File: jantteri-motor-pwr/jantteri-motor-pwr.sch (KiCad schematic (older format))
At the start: 0 parts

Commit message: jantteri-pwr-motor
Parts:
- added F1: C58066, Fuse:Fuseholder_Cylinder-5x20mm_Stelvio-Kontek_PTF78_Horizontal_Open, symbol Device:Fuse_Small
- added FB1: GZ2012D101TF, Inductor_SMD:L_0805_2012Metric, symbol Device:Ferrite_Bead
- added H1, H2, H3, H4: MountingHole_Pad, MountingHole:MountingHole_3.2mm_M3_Pad_Via, symbol Mechanical:MountingHole_Pad
- added J1: Conn_01x06_Male, Connector_JST2:JST_ZH_B6B-ZR_1x06_P1.50mm_Vertical, symbol Connector:Conn_01x06_Male
- added J5: 12V, Connector_PinHeader_2.54mm:PinHeader_1x02_P2.54mm_Vertical, symbol Connector:Conn_01x02_Male
- added J6: PWR-SW, Connector_PinHeader_2.54mm:PinHeader_1x03_P2.54mm_Vertical, symbol Connector:Conn_01x03_Male
- added J7: M, Connector_PinHeader_2.54mm:PinHeader_1x02_P2.54mm_Vertical, symbol Connector:Conn_01x02_Male
- added Q1: PDN3909S, Package_TO_SOT_SMD:SOT-23, symbol Transistor_FET:Si2319CDS
- added R1, R2: 4K7, Resistor_SMD:R_0805_2012Metric, symbol Device:R_Small
- added U1: lora-mod, voja-footprints:lora-mod, symbol voja-lib:lora-mod
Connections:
- net labels added: +3.3V, DRV_FAULT, DRV_SLEEP, HIT_INT, LORA_INT, M+, M-, MOTOR_A, MOTOR_B, POT, PWR+, SCL, SDA, USB-5V
- net labels removed: +3V3
- wire segments 8 -> 55
- no-connect marks 0 -> 2

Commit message: revised motor-pwr
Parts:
- U1: symbol voja-lib:lora-mod -> jantteri-motor-pwr-rescue:lora-mod-voja-lib
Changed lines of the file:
@@
 	2500 3750 2550 3750
 $Comp
-L voja-lib:lora-mod U1
+L jantteri-motor-pwr-rescue:lora-mod-voja-lib U1
 U 1 1 611C29AF
 P 8700 4200

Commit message: random changes
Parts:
- removed F1: C58066, Fuse:Fuseholder_Cylinder-5x20mm_Stelvio-Kontek_PTF78_Horizontal_Open, symbol Device:Fuse_Small
- Q1: value PDN3909S -> AO3401A; LCSC C441843 -> C700954
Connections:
- net PWR+: now also J6.2 (Pin_2)
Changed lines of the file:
@@
 AR Path="/612244CD/611DB1A0" Ref="Q?"  Part="1"
 F 0 "Q1" V 1492 1250 50  0000 C CNN
-F 1 "PDN3909S" V 1401 1250 50  0000 C CNN
+F 1 "AO3401A" V 1401 1250 50  0000 C CNN
 F 2 "Package_TO_SOT_SMD:SOT-23" H 1350 1175 50  0001 L CIN
 F 3 "http://www.vishay.com/docs/66709/si2319cd.pdf" H 1150 1250 50  0001 L CNN
-F 4 "C441843" V 1150 1250 50  0001 C CNN "LCSC"
+F 4 "C700954" V 1150 1250 50  0001 C CNN "LCSC"
 	1    1150 1250
 	0    -1   -1   0
@@
 	1    0    0    -1
 $EndComp
-$Comp
-L Device:Fuse_Small F1
-U 1 1 611FF9F7
-P 7750 2150
-F 0 "F1" H 7750 2335 50  0000 C CNN
-F 1 "C58066" H 7750 2244 50  0000 C CNN
-F 2 "Fuse:Fuseholder_Cylinder-5x20mm_Stelvio-Kontek_PTF78_Horizontal_Open" H 7750 2150 50  0001 C CNN
-F 3 "~" H 7750 2150 50  0001 C CNN
-F 4 "C58066" H 7750 2150 50  0001 C CNN "LCSC"
-	1    7750 2150
-	1    0    0    -1
-$EndComp
 Wire Wire Line
 	7200 2250 7500 2250
@@
 Wire Wire Line
 	7750 1600 7750 1700
-Wire Wire Line
-	7200 2150 7650 2150
-Wire Wire Line
-	7850 2150 8100 2150
 $Comp
 L Connector:Conn_01x02_Male J7
@@
 	1    0    0    -1
 $EndComp
+Wire Wire Line
+	7200 2150 8100 2150
 $EndSCHEMATC

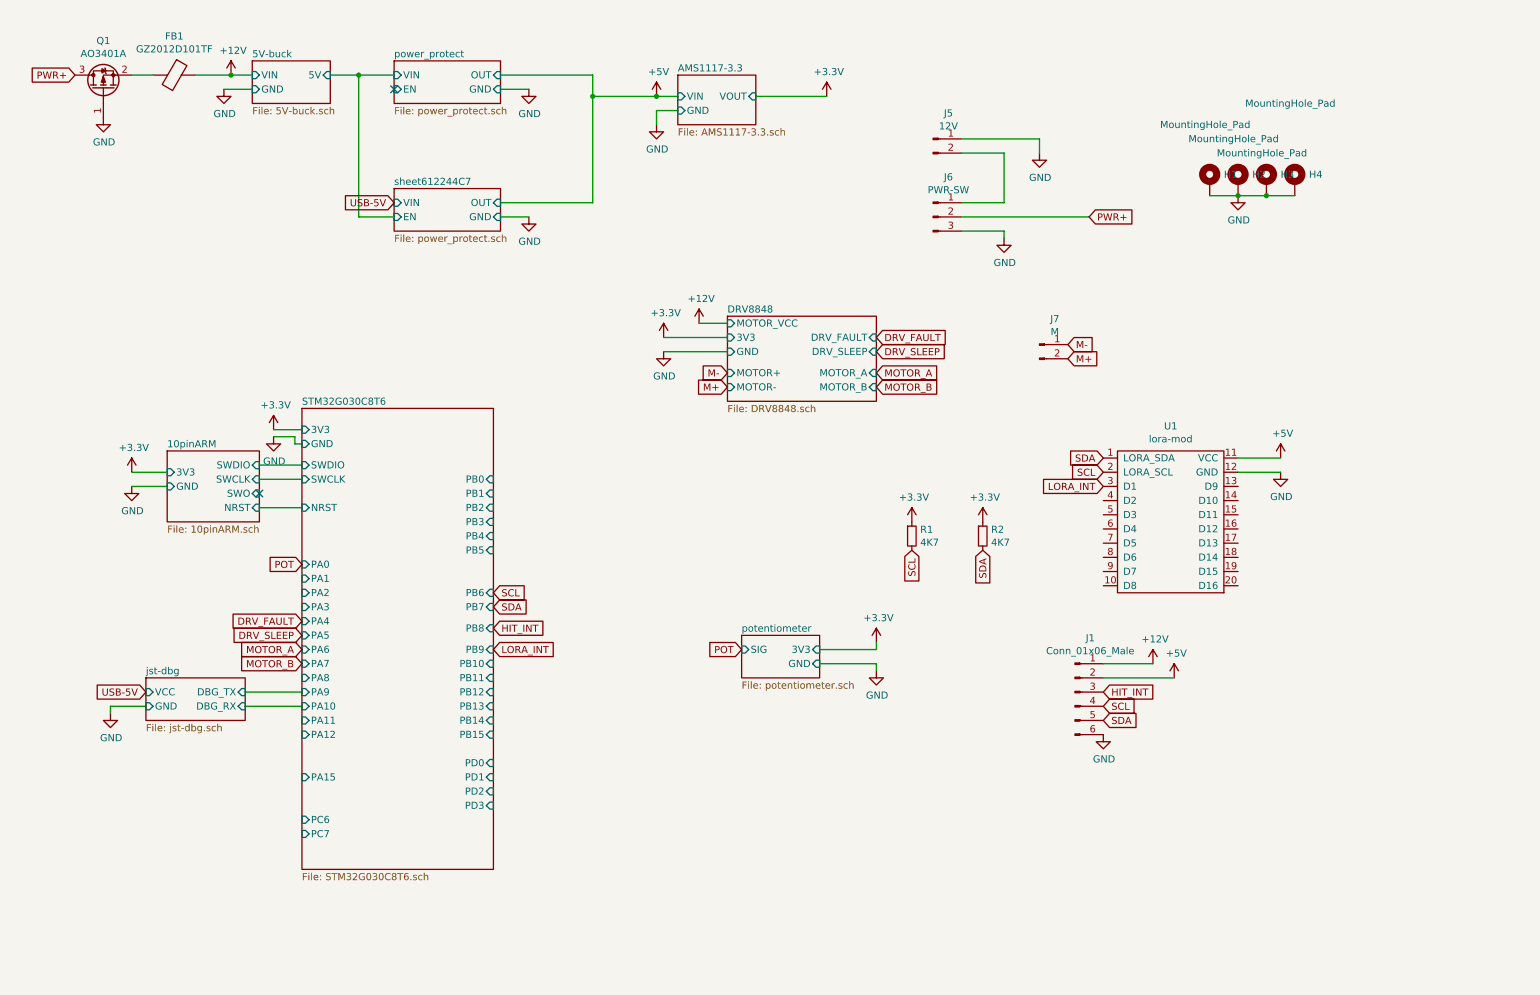
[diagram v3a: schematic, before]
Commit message: Tuubijantteri design Ordered
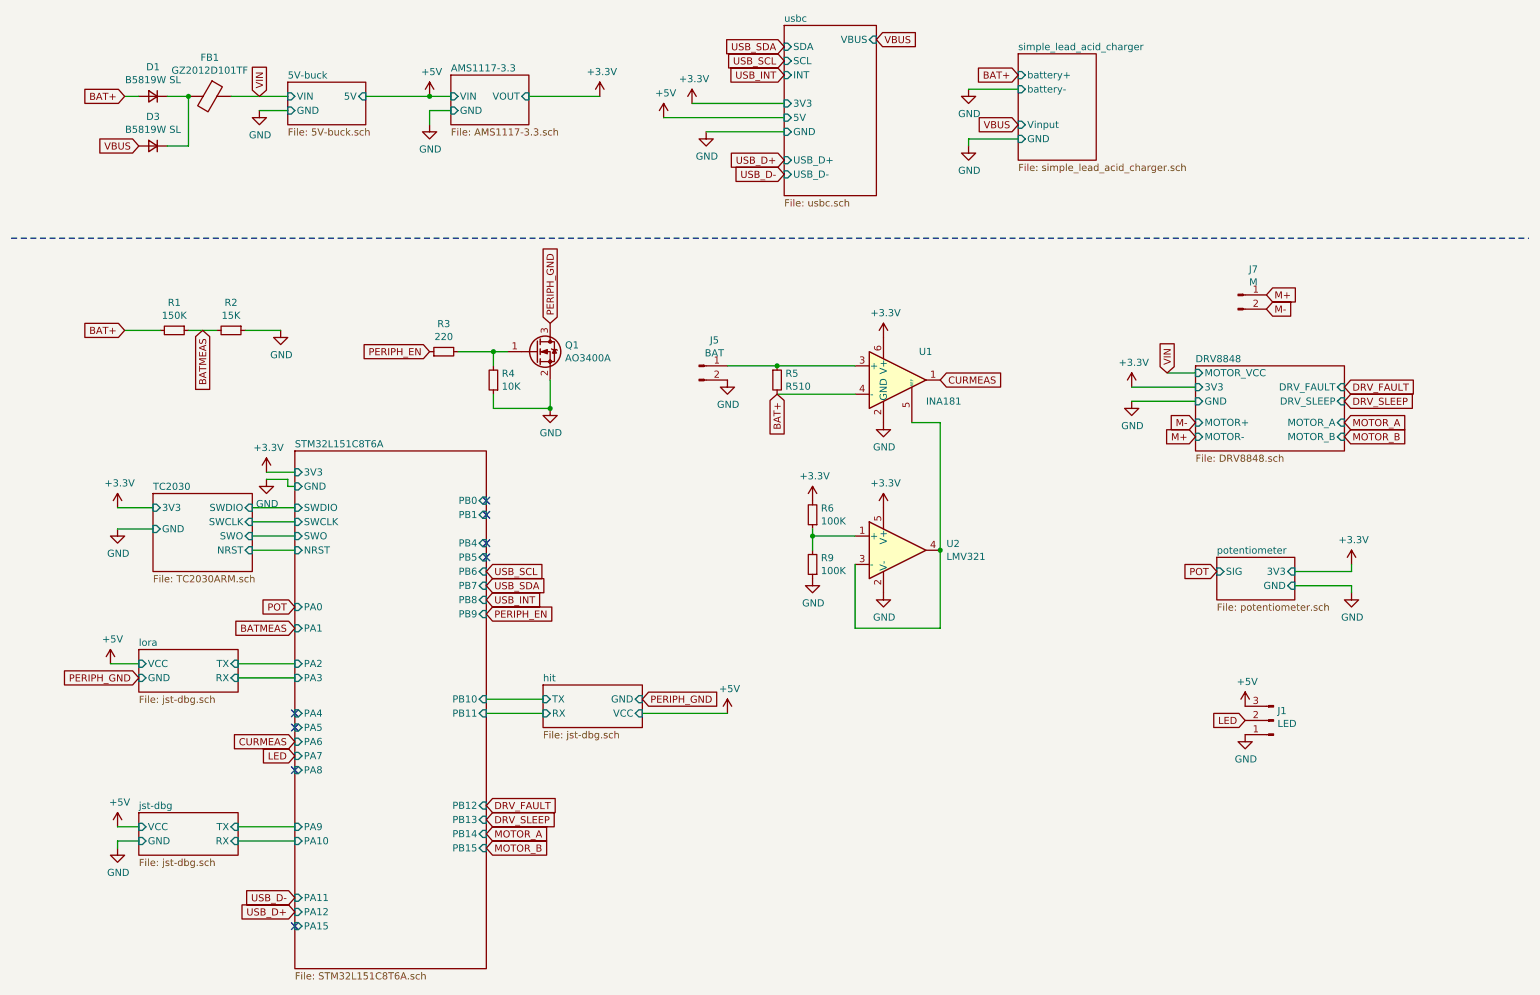
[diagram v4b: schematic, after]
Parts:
- removed H1, H2, H3, H4: MountingHole_Pad, MountingHole:MountingHole_3.2mm_M3_Pad_Via, symbol Mechanical:MountingHole_Pad
- removed J1: Conn_01x06_Male, Connector_JST2:JST_ZH_B6B-ZR_1x06_P1.50mm_Vertical, symbol Connector:Conn_01x06_Male
- removed J6: PWR-SW, Connector_PinHeader_2.54mm:PinHeader_1x03_P2.54mm_Vertical, symbol Connector:Conn_01x03_Male
- removed Q1: AO3401A, Package_TO_SOT_SMD:SOT-23, symbol Transistor_FET:Si2319CDS
- removed U1: lora-mod, voja-footprints:lora-mod, symbol jantteri-motor-pwr-rescue:lora-mod-voja-lib
- added D1, D3: B5819W SL, Diode_SMD:D_SOD-123, symbol Device:D_Small
- added J1: LED, Connector_JST2:JST_ZH_B3B-ZR_1x03_P1.50mm_Vertical, symbol Connector:Conn_01x03_Male
- added Q1: AO3400A, Package_TO_SOT_SMD:SOT-23, symbol Transistor_FET:AO3400A
- added R3: 220, Resistor_SMD:R_0402_1005Metric, symbol Device:R_Small
- added R4: 10K, Resistor_SMD:R_0402_1005Metric, symbol Device:R_Small
- added R5: R510, Resistor_SMD:R_2512_6332Metric, symbol Device:R_Small
- added R6, R9: 100K, Resistor_SMD:R_0402_1005Metric, symbol Device:R_Small
- added U1: INA181, Package_TO_SOT_SMD:SOT-23-6, symbol Amplifier_Current:INA181
- added U2: LMV321, Package_TO_SOT_SMD:SOT-23-5, symbol Amplifier_Operational:LMV321
- J5: value 12V -> BAT; footprint Connector_PinHeader_2.54mm:PinHeader_1x02_P2.54mm_Vertical -> Connector_JST2:JST_VH_B2PS-VH_1x02_P3.96mm_Horizontal
- J7: footprint Connector_PinHeader_2.54mm:PinHeader_1x02_P2.54mm_Vertical -> Connector_JST2:JST_VH_B2PS-VH_1x02_P3.96mm_Horizontal
- R1: value 4K7 -> 150K; footprint Resistor_SMD:R_0805_2012Metric -> Resistor_SMD:R_0402_1005Metric; LCSC C17673 -> C25755
- R2: value 4K7 -> 15K; footprint Resistor_SMD:R_0805_2012Metric -> Resistor_SMD:R_0402_1005Metric; LCSC C17673 -> C25756
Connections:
- net +3V3: now also R6.2, U1.6 (V+), U2.5 (V+); no longer R1.1, R2.1
- net +5V: now also J1.3 (Pin_3)
- net GND: now also J5.2 (Pin_2), R2.1, J1.1 (Pin_1), Q1.2 (S), R4.1, R9.1, U1.2 (GND), U2.2 (V-); no longer J5.1 (Pin_1)
- net M+: now also J7.1 (Pin_1); no longer J7.2 (Pin_2)
- net M-: now also J7.2 (Pin_2); no longer J7.1 (Pin_1)
- net at FB1.2: now also D1.1 (K), D3.1 (K)
- net +12V renamed VIN
- net SCL renamed BAT+
- net BAT+: now also D1.2 (A), R5.2, U1.4 (-)
- net SDA renamed BATMEAS
- net BATMEAS: now also R1.1
- new net: J5.1 (Pin_1), R5.1, U1.3 (+)
- new net: Q1.1 (G), R3.2, R4.2
- new net: U1.5 (REF), U2.3 (-), U2.4
- new net: R6.1, R9.2, U2.1 (+)
- new net CURMEAS: U1.1
- new net LED: J1.2 (Pin_2)
- new net PERIPH_EN: R3.1
- new net PERIPH_GND: Q1.3 (D)
- new net VBUS: D3.2 (A)
- no-connect marks 2 -> 8
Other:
- moved on the sheet: FB1, J5, J7
